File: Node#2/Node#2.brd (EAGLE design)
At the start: 60.5 x 120 mm, 135 parts, among them IC1 TSL25911FN, J1 68712414522, Q1 BC847ALT1SMD, Q2 SI1308EDL-T1-GE3, Q3 FDN304PZ, U2 RV8564C3, U3 BLUENRG-232, U4 TPS63001DRCT, Y3 ECS-160-12-36-AGN-TR, Y4 NX2012SA-32.768K-STD-MUB-1

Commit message: display
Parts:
- moved ANT2 143.5 mm to (43.4, 105.8)
- moved C53 143.5 mm to (43.4, 89.6)
- moved C54 143.5 mm to (45.2, 89.6)
- moved C55 143.5 mm to (38.6, 102.8)
- moved C56 143.5 mm to (36.8, 102.8)
- moved C57 143.5 mm to (47.2, 100.0)
- moved C58 143.5 mm to (50.0, 99.2)
- moved C60 143.5 mm to (49.5, 93.4)
- moved C61 143.5 mm to (53.3, 95.4)
- moved C62 143.5 mm to (55.1, 95.4)
- moved C63 143.5 mm to (53.8, 101.8)
- moved C64 143.5 mm to (31.7, 99.0)
- moved C65 143.5 mm to (33.0, 104.1)
- moved C66 143.5 mm to (48.7, 102.0)
- moved C68 143.5 mm to (31.0, 84.5)
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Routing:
- net +3V3: track 300.1 -> 333.1 mm, vias 13 -> 15
- net VGL: track 0.00 -> 30.3 mm, vias 0 -> 2
- net VGH: track 0.00 -> 29.0 mm, vias 0 -> 2
- net VSS: track 0.00 -> 26.6 mm, vias 0 -> 2
- net DC: track 0.00 -> 26.6 mm, vias 0 -> 2
- net BUSY_N: track 0.00 -> 23.8 mm, vias 0 -> 2
- net DIO2: track 2.00 -> 23.7 mm
- net DIO0: track 0.00 -> 18.4 mm
- net DIO1: track 0.00 -> 13.6 mm, vias 0 -> 2
- net GDR: track 0.00 -> 12.4 mm, vias 0 -> 1
- net BS: track 0.00 -> 11.2 mm
- net N$23: track 0.00 -> 11.0 mm
- net VCOM: track 0.00 -> 10.4 mm
- net RESE: track 0.00 -> 9.61 mm, vias 0 -> 2
- net VSHR: track 0.00 -> 9.20 mm
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
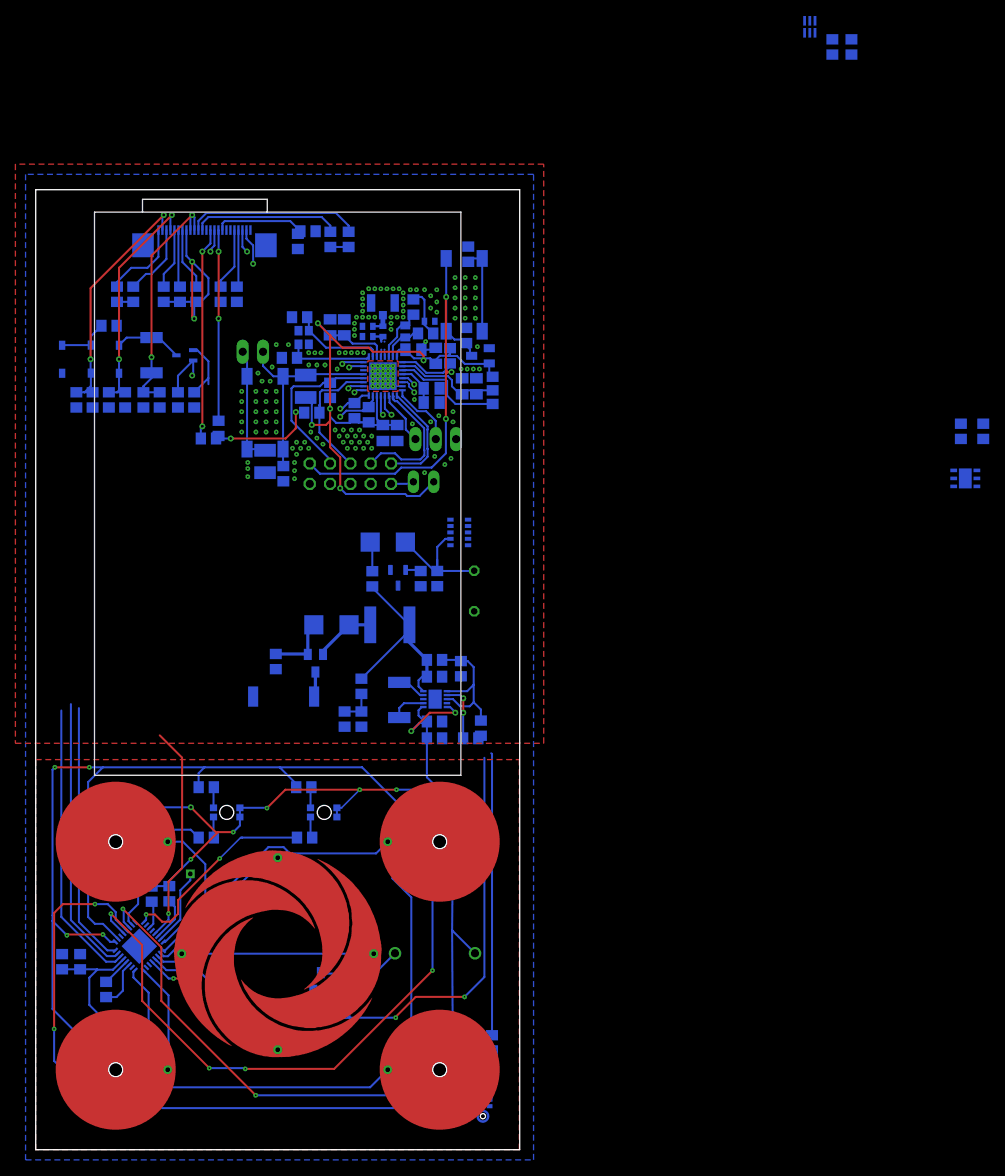
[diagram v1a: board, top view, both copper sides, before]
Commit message: Finished Layout Node#2
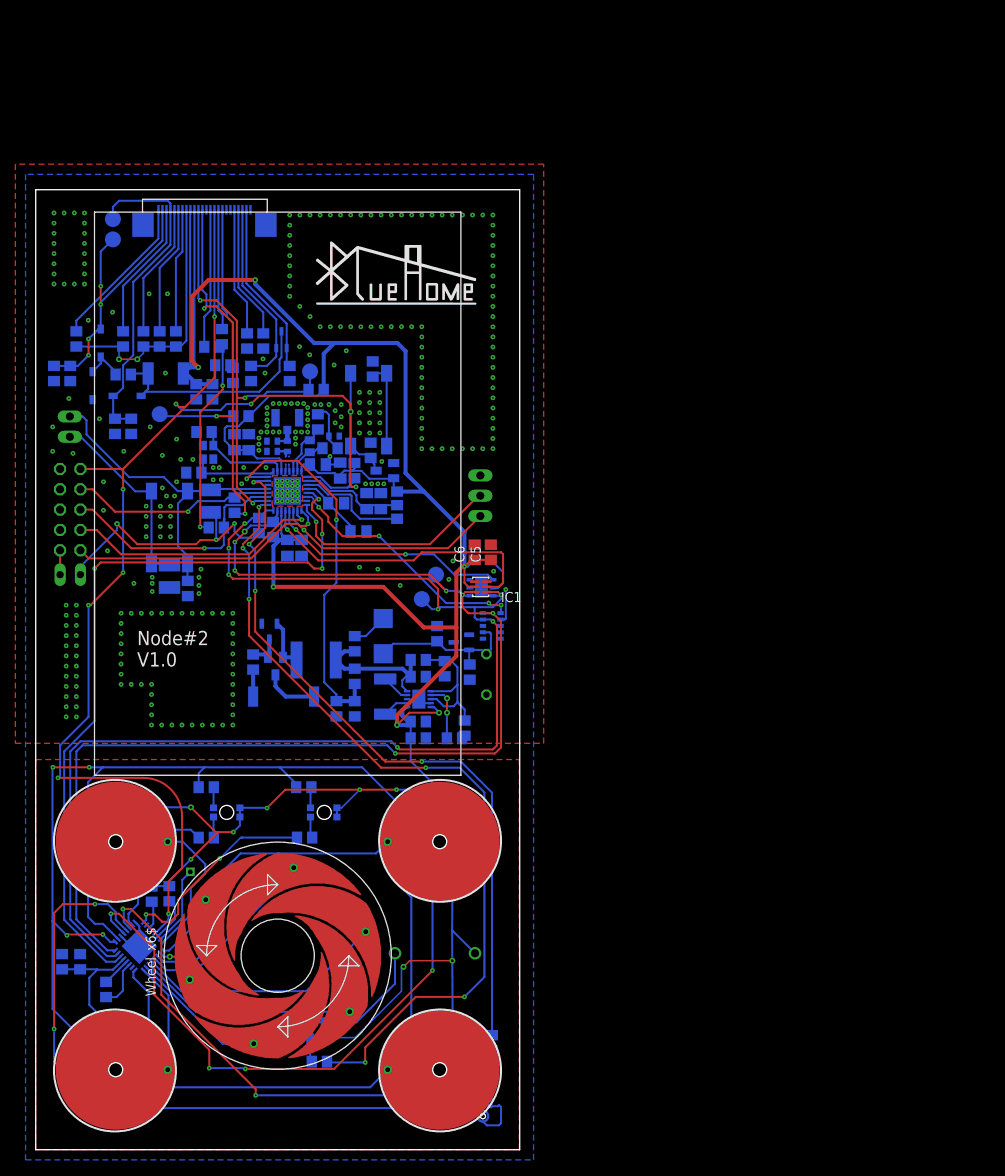
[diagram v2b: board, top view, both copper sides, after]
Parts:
- removed D1: ZENER_SMB, BlueHome:SMB
- removed U$7: PROXIMITY, BlueHome:PROXIMITY
- removed U$8: WHEEL, BlueHome:WHEEL
- added PROXI: PROXIMITY, BlueHome:PROXIMITY
- added TP1, TP2, TP3, TP4, TP5, TP6: PTR1TP20R, testpad:TP20R
- added U$18: BZB984_5.4V, BlueHome:SOT95P230X110-3N
- added U$19: WHEEL6, BlueHome:WHEEL6
- moved IC1 81.2 mm to (55.6, 70.4), flipped to the top, turned to 180 degrees
- moved C6 78.8 mm to (54.9, 74.7), flipped to the top
- moved C5 76.2 mm to (56.9, 74.7), flipped to the top
- moved C13 65.4 mm to (54.9, 74.7), turned to 90 degrees
- moved HM1 62.0 mm to (55.7, 70.2)
- moved C12 60.7 mm to (56.9, 74.7), turned to 90 degrees
- moved JP5 45.7 mm to (4.32, 71.9)
- moved JP3 35.3 mm to (4.32, 80.0), turned to 90 degrees
- moved R8 24.8 mm to (25.7, 91.7), turned to 180 degrees
- moved JP8 24.7 mm to (4.27, 90.4), turned to 270 degrees
- moved R3 19.2 mm to (35.1, 95.0), turned to 180 degrees
- moved ANT2 18.7 mm to (31.5, 91.5)
- moved C53 18.7 mm to (31.5, 75.2)
- moved C55 18.7 mm to (26.6, 88.4)
- moved C56 18.7 mm to (24.9, 88.4)
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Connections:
- removed net PROX_SENS: U$2.31, U$7.P$1
- removed net SEG4: U$2.5, U$8.SEG4
- new net PROX: PROXI.P$1, U$2.31
- new net PROXI: U$19.SEG4, U$2.5
- net DIO0: now also TP5.TP
- net DIO2: now also TP1.TP
- net N$14: now also U$18.3; no longer D1.A
- net N$8: now also U$18.2; no longer D1.C
- net SCL: now also TP6.TP
- net SDA: now also TP4.TP
- net SEG1: now also U$19.SEG1; no longer U$8.SEG1
- net SEG2: now also U$19.SEG2; no longer U$8.SEG2
- net SEG3: now also U$19.SEG3; no longer U$8.SEG3
- net SEG5: now also U$19.SEG5
- net SEG6: now also U$19.SEG6
- net VGH: now also TP2.TP
- net VGL: now also TP3.TP
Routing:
- net +3V3: track 333.1 -> 512.2 mm, vias 15 -> 17
- net SCL: track 39.9 -> 159.1 mm, vias 1 -> 7
- net SDA: track 38.5 -> 151.7 mm, vias 1 -> 7
- net RESETN: track 92.2 -> 176.4 mm, vias 5 -> 10
- net DIO13: track 37.7 -> 95.6 mm, vias 1 -> 4
- net DIO3: track 48.4 -> 104.3 mm, vias 3 -> 6
- net ADC1: track 37.1 -> 91.1 mm, vias 1 -> 4
- net ADC2: track 7.04 -> 47.8 mm, vias 1 -> 2
- net DIO0: track 18.4 -> 54.5 mm, vias 0 -> 3
- net DIO6: track 2.49 -> 37.4 mm
- net PROXI: track 0.00 -> 31.3 mm
- net DIO2: track 23.7 -> 54.4 mm, vias 1 -> 3
- net DIO12: track 2.25 -> 31.5 mm, vias 1 -> 4
- net SEG5: track 0.00 -> 27.5 mm
- net DIO7: track 2.86 -> 30.1 mm, vias 1 -> 2
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- added copper zone on layer 1, net PROX
- removed copper zone on layer 1, net PROX_SENS
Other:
- board text added: "Node#2 V1.0"

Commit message: finished again
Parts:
- D2: value (none) -> DIODE1210; device eagle-ltspice:DIODE_SMB -> BlueHome:C1210
- R2: value 100 -> 1M
- moved U$15 0.65 mm to (37.4, 89.8)
- moved C66 0.63 mm to (36.8, 88.3)
- moved C58 0.13 mm to (38.1, 84.8)
- moved LED6 0.07 mm to (36.1, 42.2)
- turned D2 to 270 degrees
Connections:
- net +3V3_RTC: now also D2.2; no longer D2.C
- net N$1: now also D2.1; no longer D2.A
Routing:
- net GND: track 27.7 -> 29.4 mm, vias 302 -> 303
- net SCL: track 159.1 -> 158.4 mm
- net N$52: track 6.32 -> 5.69 mm

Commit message: beautyfied
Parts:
- L1, L2: device rcl:L5038P -> BlueHome:L5038P
- moved TP5 3.53 mm to (17.7, 89.2)
- moved L2 1.27 mm to (16.3, 95.8), turned to 270 degrees
- moved L1 0.57 mm to (43.2, 56.9)
- moved C58 0.25 mm to (38.1, 85.0)
- moved C26 0.18 mm to (10.8, 97.0)
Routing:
- net N$2: track 6.27 -> 0.00 mm
- net GND: track 29.4 -> 23.4 mm, vias 303 -> 305
- net RESETN: track 176.4 -> 174.7 mm
- net +3V3: track 512.1 -> 513.4 mm
- net L1: track 3.57 -> 4.49 mm
- net VSS: track 34.0 -> 34.9 mm
- net DIO0: track 54.5 -> 53.8 mm
- net L2: track 3.30 -> 3.99 mm
- net V+: track 18.8 -> 19.5 mm

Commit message: print version
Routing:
- net +3V3: track 513.4 -> 472.8 mm
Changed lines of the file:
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@@
 <?xml version="1.0" encoding="utf-8"?>
 <!DOCTYPE eagle SYSTEM "eagle.dtd">
-<eagle version="9.3.0">
+<eagle version="9.2.1">
 <drawing>
 <settings>
@@
 <wire x1="40.70373125" y1="84.8654" x2="41.69913125" y2="83.87" width="0.254" layer="16"/>
 <wire x1="41.69913125" y1="83.87" x2="44.748" y2="83.87" width="0.254" layer="16"/>
-<contactref element="LED1" pad="3"/>
-<contactref element="LED1" pad="4"/>
 <wire x1="11.55" y1="37.925" x2="11.55" y2="39.075" width="0.254" layer="16"/>
-<contactref element="LED2" pad="3"/>
-<contactref element="LED2" pad="4"/>
-<wire x1="52.15" y1="37.925" x2="52.15" y2="39.075" width="0.254" layer="16"/>
-<contactref element="LED3" pad="3"/>
-<contactref element="LED3" pad="4"/>
-<contactref element="LED4" pad="3"/>
-<contactref element="LED4" pad="4"/>
-<contactref element="LED6" pad="4"/>
-<contactref element="LED5" pad="4"/>
-<contactref element="LED6" pad="3"/>
-<contactref element="LED5" pad="3"/>
 <contactref element="U$2" pad="13"/>
-<wire x1="52.15" y1="37.925" x2="52.05" y2="27.4" width="0.254" layer="16"/>
 <wire x1="52.05" y1="27.4" x2="52.072446875" y2="23.623525" width="0.254" layer="16"/>
-<wire x1="52.072446875" y1="23.623525" x2="52.15" y2="10.575" width="0.254" layer="16"/>
-<wire x1="52.15" y1="10.575" x2="52.15" y2="9.425" width="0.254" layer="16"/>
 <wire x1="11.55" y1="9.425" x2="11.55" y2="10.668" width="0.254" layer="16"/>
 <wire x1="11.55" y1="10.668" x2="11.55" y2="13.25" width="0.254" layer="16"/>
@@
 <wire x1="15.775" y1="5.2" x2="52.55" y2="5.2" width="0.254" layer="16"/>
 <wire x1="15.775" y1="5.2" x2="11.55" y2="9.425" width="0.254" layer="16"/>
-<wire x1="52.15" y1="39.075" x2="52.15" y2="43.3" width="0.254" layer="16"/>
-<wire x1="25.526" y1="41.589" x2="25.526" y2="42.739" width="0.254" layer="16"/>
 <wire x1="19.4" y1="36.3" x2="16.7" y2="33.6" width="0.254" layer="16"/>
 <wire x1="16.7" y1="33.6" x2="16.7" y2="32.95" width="0.254" layer="16"/>
@@
 <via x="24.7" y="39.7" extent="1-16" drill="0.2032"/>
 <wire x1="24.7" y1="39.7" x2="25.526" y2="40.526" width="0.254" layer="16"/>
-<wire x1="25.526" y1="40.526" x2="25.526" y2="41.589" width="0.254" layer="16"/>
 <via x="45.1" y="45" extent="1-16" drill="0.2032"/>
-<wire x1="25.526" y1="42.739" x2="28.861" y2="42.739" width="0.254" layer="16"/>
 <wire x1="28.861" y1="42.739" x2="28.9" y2="42.7" width="0.254" layer="16"/>
 <via x="28.9" y="42.7" extent="1-16" drill="0.2032"/>
 <wire x1="28.9" y1="42.7" x2="31.2" y2="45" width="0.254" layer="1"/>
 <wire x1="31.2" y1="45" x2="40.5" y2="45" width="0.254" layer="1"/>
-<wire x1="37.718" y1="42.737259375" x2="38.237259375" y2="42.737259375" width="0.254" layer="16"/>
 <wire x1="54.912" y1="24.56" x2="52.072" y2="27.4" width="0.254" layer="16"/>
 <wire x1="52.072" y1="27.4" x2="52.05" y2="27.4" width="0.254" layer="16"/>
@@
 <wire x1="22.5" y1="39.7" x2="22.8" y2="39.7" width="0.2032" layer="1"/>
 <wire x1="55.3" y1="9.95" x2="54.775" y2="9.425" width="0.254" layer="16"/>
-<wire x1="54.775" y1="9.425" x2="52.15" y2="9.425" width="0.254" layer="16"/>
 <wire x1="53.2" y1="5.85" x2="53.611" y2="6.261" width="0.254" layer="16"/>
 <wire x1="45.8228" y1="54.2692" x2="46.566" y2="53.526" width="0.508" layer="16"/>
@@
 <wire x1="53.2" y1="5.85" x2="53.2" y2="7.15" width="0.254" layer="16"/>
 <wire x1="53.2" y1="7.15" x2="52.05" y2="8.3" width="0.254" layer="16"/>
-<wire x1="52.15" y1="9.425" x2="52.05" y2="9.325" width="0.254" layer="16"/>
 <wire x1="52.05" y1="9.325" x2="52.05" y2="8.3" width="0.254" layer="16"/>
 <wire x1="46.866" y1="51.426" x2="46.866" y2="48.584" width="0.254" layer="16"/>
@@
 <wire x1="46.737525" y1="23.623525" x2="52.072446875" y2="23.623525" width="0.2032" layer="1"/>
 <via x="52.072446875" y="23.623525" extent="1-16" drill="0.35"/>
-<wire x1="11.65" y1="9.425" x2="11.55" y2="9.425" width="0.2032" layer="16"/>
-<wire x1="11.65" y1="10.575" x2="11.557" y2="10.668" width="0.2032" layer="16"/>
 <wire x1="11.557" y1="10.668" x2="11.55" y2="10.668" width="0.2032" layer="16"/>
-<wire x1="11.65" y1="39.075" x2="11.55" y2="39.075" width="0.2032" layer="16"/>
-<wire x1="11.65" y1="37.925" x2="11.55" y2="37.925" width="0.2032" layer="16"/>
 <wire x1="58.42" y1="72.202" x2="56.896" y2="73.726" width="0.254" layer="16"/>
 <wire x1="56.896" y1="73.726" x2="54.864" y2="73.726" width="0.254" layer="16"/>
-<wire x1="37.718" y1="42.737259375" x2="37.718" y2="41.587259375" width="0.254" layer="16"/>
 <wire x1="16.256" y1="98.358" x2="17.466" y2="98.358" width="0.508" layer="16"/>
 <wire x1="20.066" y1="95.758" x2="20.066" y2="95.692" width="0.508" layer="16"/>
@@
 <wire x1="19.841" y1="98.904" x2="19.841" y2="117.496" width="0.254" layer="16"/>
 <contactref element="MK1" pad="5"/>
-<wire x1="53.611" y1="6.261" x2="55.0625" y2="6.261" width="0" layer="19" extent="16-16"/>
+<contactref element="LED6" pad="3"/>
+<contactref element="LED5" pad="3"/>
+<contactref element="LED2" pad="3"/>
+<contactref element="LED6" pad="4"/>
+<contactref element="LED4" pad="3"/>
+<contactref element="LED3" pad="3"/>
+<contactref element="LED3" pad="4"/>
+<contactref element="LED4" pad="4"/>
+<contactref element="LED1" pad="4"/>
+<contactref element="LED1" pad="3"/>
+<contactref element="LED2" pad="4"/>
+<contactref element="LED5" pad="4"/>
+<wire x1="52.15" y1="37.925" x2="52.15" y2="39.075" width="0" layer="19" extent="16-16"/>
+<wire x1="52.15" y1="43.3" x2="52.15" y2="39.075" width="0" layer="19" extent="16-16"/>
+<wire x1="37.718" y1="42.737259375" x2="38.237259375" y2="42.737259375" width="0" layer="19" extent="16-16"/>
+<wire x1="37.718" y1="41.587259375" x2="37.718" y2="42.737259375" width="0" layer="19" extent="16-16"/>
+<wire x1="25.526" y1="42.739" x2="28.861" y2="42.739" width="0" layer="19" extent="16-16"/>
+<wire x1="25.526" y1="41.589" x2="25.526" y2="42.739" width="0" layer="19" extent="16-16"/>
+<wire x1="25.526" y1="40.526" x2="25.526" y2="41.589" width="0" layer="19" extent="16-16"/>
+<wire x1="11.65" y1="39.075" x2="11.55" y2="39.075" width="0" layer="19" extent="16-16"/>
+<wire x1="11.65" y1="37.925" x2="11.55" y2="37.925" width="0" layer="19" extent="16-16"/>
+<wire x1="11.005915625" y1="23.85380625" x2="14.5" y2="32.9" width="0" layer="19" extent="16-16"/>
+<wire x1="11.65" y1="9.425" x2="11.55" y2="9.425" width="0" layer="19" extent="16-16"/>
+<wire x1="52.15" y1="9.425" x2="52.05" y2="9.325" width="0" layer="19" extent="16-16"/>
+<wire x1="11.65" y1="10.575" x2="11.55" y2="10.668" width="0" layer="19" extent="16-16"/>
+<wire x1="52.15" y1="10.575" x2="52.15" y2="9.425" width="0" layer="19" extent="16-16"/>
+<wire x1="55.0625" y1="6.261" x2="53.611" y2="6.261" width="0" layer="19" extent="16-16"/>
+<wire x1="54.775" y1="9.425" x2="52.15" y2="9.425" width="0" layer="19" extent="16-16"/>
+<wire x1="52.072" y1="27.4" x2="52.15" y2="37.925" width="0" layer="19" extent="16-16"/>
 </signal>
 <signal name="N$14">
